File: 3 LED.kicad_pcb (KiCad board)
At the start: 2 copper layers, 24 x 48 mm, 14 parts, among them J1 Conn_01x04_Socket, Q1 NPN, Q2 NPN, Q3 NPN, U1 74HC238

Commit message: On Production
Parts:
- removed the G*** at (105.0, 133.5)
- removed U2, U3: ~, Library_Custom:LEGO HOLE 4.5-6.5
- added C1: C, Capacitor_SMD:C_0805_2012Metric, B.Cu at (149.5, 95.2)
- added G***: LOGO, DeltaKiteEngineering:BKU_Medium, B.Cu at (148.0, 72.5)
- added G***: LOGO, DeltaKiteEngineering:DeltaKite_Large, B.Cu at (148.0, 65.0)
- added REF**: Module Base, Library_Custom:Module Base, F.Cu at (142.2, 111.8)
- moved R3 45.2 mm to (141.2, 74.0)
- moved U1 45.0 mm to (141.2, 95.2), turned to -90 degrees
- moved D1 42.1 mm to (140.2, 89.5), turned to 0 degrees
- moved J1 41.6 mm to (141.2, 102.1)
- moved D2 41.5 mm to (140.2, 77.5), turned to 0 degrees
- moved D3 41.0 mm to (140.2, 65.5), turned to 0 degrees
- moved R1 39.8 mm to (141.2, 86.0)
- moved Q3 37.8 mm to (132.2, 91.5)
- moved R2 32.7 mm to (141.2, 81.0)
- moved Q2 32.0 mm to (132.2, 96.0)
- moved Q1 23.2 mm to (132.2, 100.8)
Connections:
- R2 pad 2: Net-(D3-A) -> Net-(D2-A)
- R3 pad 2: Net-(D2-A) -> Net-(D3-A)
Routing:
- net +5V: track 130.4 -> 40.3 mm
- net /L3: track 39.8 -> 11.8 mm
- net /L1: track 21.9 -> 8.18 mm, vias 2 -> 0
- net GND: track 70.6 -> 58.2 mm
- net Net-(Q3-E): track 20.5 -> 31.1 mm, vias 0 -> 2
- net Net-(D2-A): track 14.4 -> 4.46 mm
- net /L2: track 13.9 -> 22.0 mm
- net Net-(Q1-E): track 39.8 -> 44.7 mm, vias 0 -> 2
- net Net-(Q2-E): track 28.1 -> 24.6 mm
- net Net-(D3-A): track 12.4 -> 9.46 mm
- net /S0: track 9.29 -> 12.0 mm
- net Net-(D1-A): track 6.27 -> 5.34 mm
- net /S1: track 7.62 -> 6.76 mm

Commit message: Production Version
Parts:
- removed D1, D2, D3: LED, LED_THT:LED_D10.0mm
- removed the G*** at (148.0, 65.0)
- removed J1: Conn_01x04_Socket, Library_Custom:SEEEDSTUDIO_114020164
- removed the REF** at (142.2, 111.8)
- added Groove: Conn_01x04_Socket, Library_Custom:SEEEDSTUDIO_114020164, F.Cu at (141.7, 129.8)
- added JP1: Jumper_2_Open, SofleRGB:Jumper, B.Cu at (139.0, 130.4)
- added JP2: Jumper_2_Open, SofleRGB:Jumper, B.Cu at (141.7, 130.4)
- added JP3: Jumper_2_Open, SofleRGB:Jumper, B.Cu at (144.4, 130.4)
- added LED_GREEN: LED, LED_THT:LED_D10.0mm, F.Cu at (140.5, 116.0)
- added LED_RED: LED, LED_THT:LED_D10.0mm, F.Cu at (140.5, 92.0)
- added LED_YELLOW: LED, LED_THT:LED_D10.0mm, F.Cu at (140.5, 104.0)
- added R4: R, Resistor_SMD:R_0603_1608Metric, B.Cu at (150.5, 100.1)
- added R5: R, Resistor_SMD:R_0603_1608Metric, B.Cu at (150.5, 102.6)
- added R6: R, Resistor_SMD:R_0603_1608Metric, B.Cu at (150.5, 105.1)
- added R7: R, Resistor_SMD:R_0603_1608Metric, B.Cu at (133.5, 114.5)
- added R8: R, Resistor_SMD:R_0603_1608Metric, B.Cu at (133.5, 117.0)
- added R9: R, Resistor_SMD:R_0603_1608Metric, B.Cu at (133.5, 119.5)
- added REF**: Ohstem_Base, ACLAB:Ohstem_Base_V2, F.Cu at (142.6, 116.1)
- G***: moved to F.Cu
- U1: value 74HC238 -> 74HC238D
- moved G*** 56.4 mm to (150.8, 128.8), turned to 0 degrees
- moved R1 32.6 mm to (139.7, 118.6)
- moved C1 28.5 mm to (139.7, 122.0), turned to 180 degrees
- moved R3 20.9 mm to (140.0, 94.9)
- moved R2 19.8 mm to (140.1, 100.8)
- moved U1 15.1 mm to (141.6, 110.3)
- moved Q3 13.7 mm to (145.5, 87.9)
- moved Q2 13.3 mm to (145.5, 96.3)
- moved Q1 13.3 mm to (145.5, 100.5)
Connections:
- Q1 pad 1: +5V -> Net-(JP1-A)
- Q1 pad 2: /L1 -> Net-(Q1-B)
- Q1 pad 3: Net-(Q1-E) -> GND
- Q2 pad 1: +5V -> Net-(JP2-A)
- Q2 pad 2: /L2 -> Net-(Q2-B)
- Q2 pad 3: Net-(Q2-E) -> GND
- Q3 pad 1: +5V -> Net-(JP3-B)
- Q3 pad 2: /L3 -> Net-(Q3-B)
- Q3 pad 3: Net-(Q3-E) -> GND
- R1 pad 1: Net-(Q1-E) -> Net-(D1-K)
- R1 pad 2: Net-(D1-A) -> Net-(JP1-A)
- R2 pad 1: Net-(Q2-E) -> Net-(D2-K)
- R2 pad 2: Net-(D2-A) -> Net-(JP2-A)
- R3 pad 1: Net-(Q3-E) -> Net-(D3-K)
- R3 pad 2: Net-(D3-A) -> Net-(JP3-B)
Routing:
- net Net-(JP2-A): track 0.00 -> 89.4 mm
- net Net-(JP3-B): track 0.00 -> 81.5 mm, vias 0 -> 2
- net Net-(Q3-B): track 0.00 -> 64.7 mm, vias 0 -> 3
- net Net-(JP1-A): track 0.00 -> 60.4 mm, vias 0 -> 2
- net Net-(Q2-B): track 0.00 -> 50.5 mm, vias 0 -> 3
- net /L2: track 22.0 -> 70.0 mm, vias 0 -> 2
- net Net-(Q1-E): track 44.7 -> 0.00 mm, vias 2 -> 0
- net /L1: track 8.18 -> 48.3 mm
- net Net-(Q1-B): track 0.00 -> 37.8 mm, vias 0 -> 2
- net Net-(Q3-E): track 31.1 -> 0.00 mm, vias 2 -> 0
- net Net-(Q2-E): track 24.6 -> 0.00 mm
- net /L3: track 11.8 -> 34.0 mm
- net /S1: track 6.76 -> 25.2 mm
- net GND: track 58.2 -> 74.9 mm, vias 1 -> 2
- net /S0: track 12.0 -> 26.7 mm
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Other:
- board size 24 x 48 mm -> 24 x 48.8 mm
- board text added: "-+AB"
- board text added: "AB-LED 00-OFF 01-Gre 10-Yel 11_RED"
- board text added: "ACLAB_HCMUT"
- board text added: "Traffic Light Module"
- board text added: "github.com/ACLAB-HCMUT"

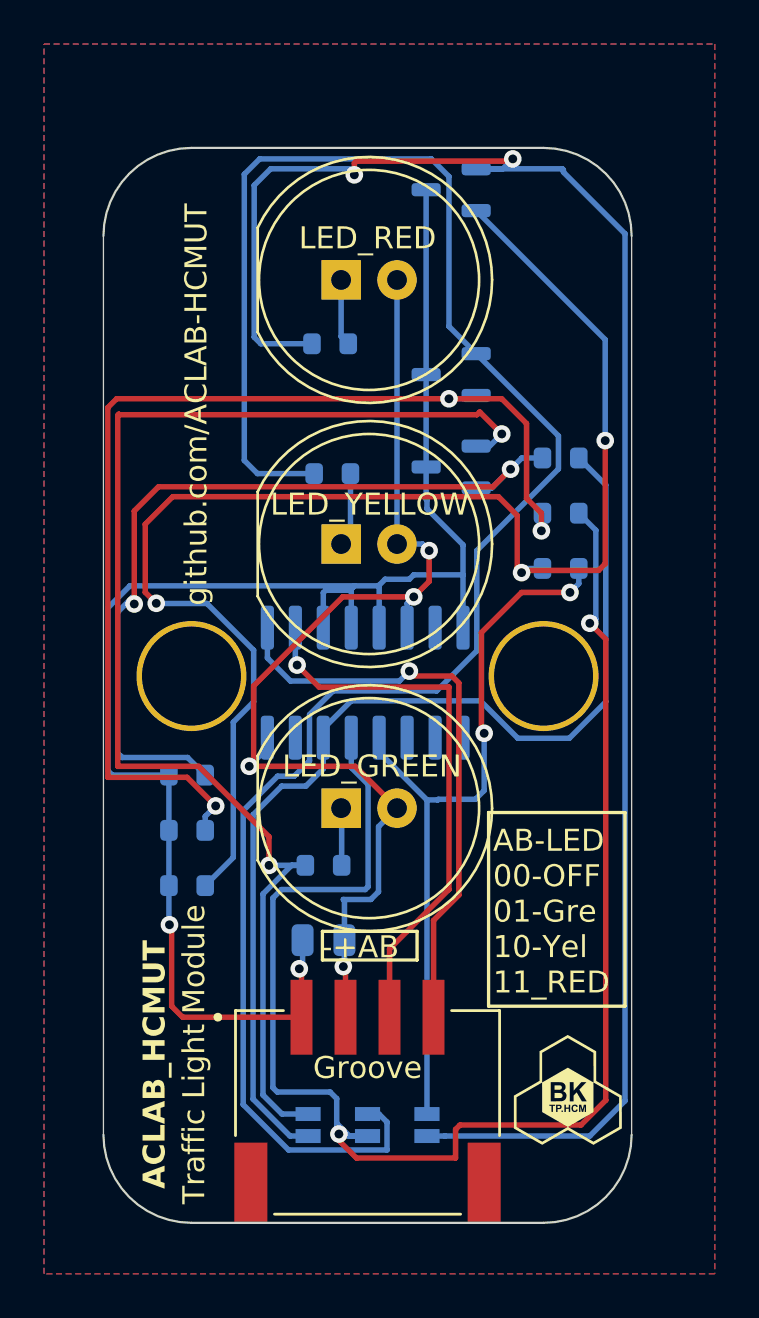
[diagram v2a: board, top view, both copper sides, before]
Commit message: update: 74HC138D
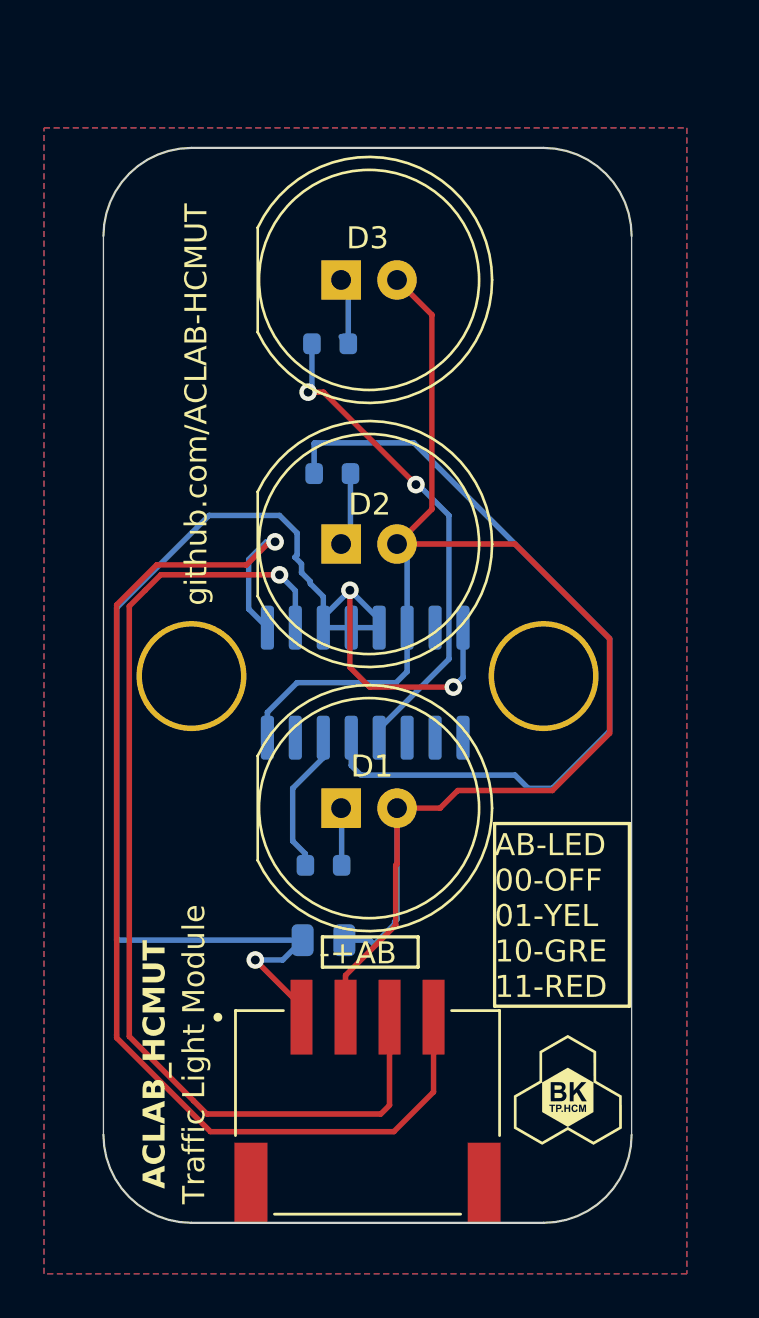
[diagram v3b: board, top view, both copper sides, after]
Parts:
- removed JP1, JP2, JP3: Jumper_2_Open, SofleRGB:Jumper
- removed Q1, Q2, Q3: NPN, Package_TO_SOT_SMD:SOT-23-3
- removed R4, R5, R6, R7, R8, R9: R, Resistor_SMD:R_0603_1608Metric
- removed U1: 74HC238D, Package_SO:SOP-16_3.9x9.9mm_P1.27mm
- added U2: 74HC138, Package_SO:SOP-16_3.9x9.9mm_P1.27mm, B.Cu at (141.6, 110.3)
- renumbered LED_GREEN to D1, LED_YELLOW to D2, LED_RED to D3, Groove to J1
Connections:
- R1 pad 2: Net-(JP1-A) -> /L1
- R2 pad 2: Net-(JP2-A) -> /L2
- R3 pad 2: Net-(JP3-B) -> /L3
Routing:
- net Net-(JP2-A): track 89.4 -> 0.00 mm
- net Net-(JP3-B): track 81.5 -> 0.00 mm, vias 2 -> 0
- net Net-(Q3-B): track 64.7 -> 0.00 mm, vias 3 -> 0
- net Net-(JP1-A): track 60.4 -> 0.00 mm, vias 2 -> 0
- net Net-(Q2-B): track 50.5 -> 0.00 mm, vias 3 -> 0
- net /L1: track 48.3 -> 7.02 mm
- net Net-(Q1-B): track 37.8 -> 0.00 mm, vias 2 -> 0
- net /L2: track 70.0 -> 37.2 mm, vias 2 -> 0
- net /S0: track 26.7 -> 53.5 mm
- net +5V: track 50.7 -> 73.4 mm, vias 4 -> 0
- net /S1: track 25.2 -> 47.1 mm
- net GND: track 74.9 -> 63.3 mm, vias 2 -> 3
- net /L3: track 34.0 -> 23.4 mm
- added copper zone on B.Cu, net (none)
- added copper zone on F.Cu, net (none)
- removed copper zone on B.Cu, net GND
- removed copper zone on F.Cu, net GND
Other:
- board text added: "AB-LED 00-OFF 01-YEL 10-GRE 11-RED"
- board text removed: "AB-LED 00-OFF 01-Gre 10-Yel 11_RED"

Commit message: update label
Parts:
- C1: value C -> 100nf
- R1, R2: value R -> 100
- R3: value R -> 160
- U2: value 74HC138 -> 74HC138D
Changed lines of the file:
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@@
         (effects (font (size 1 1) (thickness 0.15)) (justify mirror))
     )
-    (fp_text value "R" (at 0 -1.43) (layer "B.Fab")
+    (fp_text value "100" (at 0 -1.43) (layer "B.Fab")
         (effects (font (size 1 1) (thickness 0.15)) (justify mirror))
     )
@@
         (effects (font (size 1 1) (thickness 0.15)) (justify mirror))
     )
-    (fp_text value "R" (at 0 -1.43) (layer "B.Fab")
+    (fp_text value "100" (at 0 -1.43) (layer "B.Fab")
         (effects (font (size 1 1) (thickness 0.15)) (justify mirror))
     )
@@
         (effects (font (size 1 1) (thickness 0.15)) (justify mirror))
     )
-    (fp_text value "R" (at 0 -1.43) (layer "B.Fab")
+    (fp_text value "160" (at 0 -1.43) (layer "B.Fab")
         (effects (font (size 1 1) (thickness 0.15)) (justify mirror))
     )
@@
         (effects (font (size 1 1) (thickness 0.15)) (justify mirror))
     )
-    (fp_text value "74HC138" (at 0 -5.9 90) (layer "B.Fab")
+    (fp_text value "74HC138D" (at 0 -5.9 90) (layer "B.Fab")
         (effects (font (size 1 1) (thickness 0.15)) (justify mirror))
     )
@@
         (effects (font (size 1 1) (thickness 0.15)) (justify mirror))
     )
-    (fp_text value "C" (at 0 -1.68) (layer "B.Fab")
-        (effects (font (size 1 1) (thickness 0.15)) (justify mirror))
-    )
+    (fp_text value "100nf" (at 0 -1.68) (layer "B.Fab")
+        (effects (font (size 1 1) (thickness 0.15)) (justify mirror))
+    )
